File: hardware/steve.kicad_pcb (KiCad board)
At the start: 4 copper layers, 70 x 120 mm, 64 parts, among them J1 Conn_ARM_JTAG_SWD_10, J2 Micro_SD_Card_Det2, J3 TE_1-2834015-4_Buchanan_WireM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, J4 Screw_Terminal_01x04, J5 USB_C_Receptacle_16P, SW1 SW_SPST, SW2 SW_SPST, U1 STM32F407VGTx, U2 TI_TPS51386RJNR_Regulator_Buc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, U3 TLV1117LV33DCYR, U4 BMI270, U5 BMP388, Y1 12MHz, Y2 32.768kHz

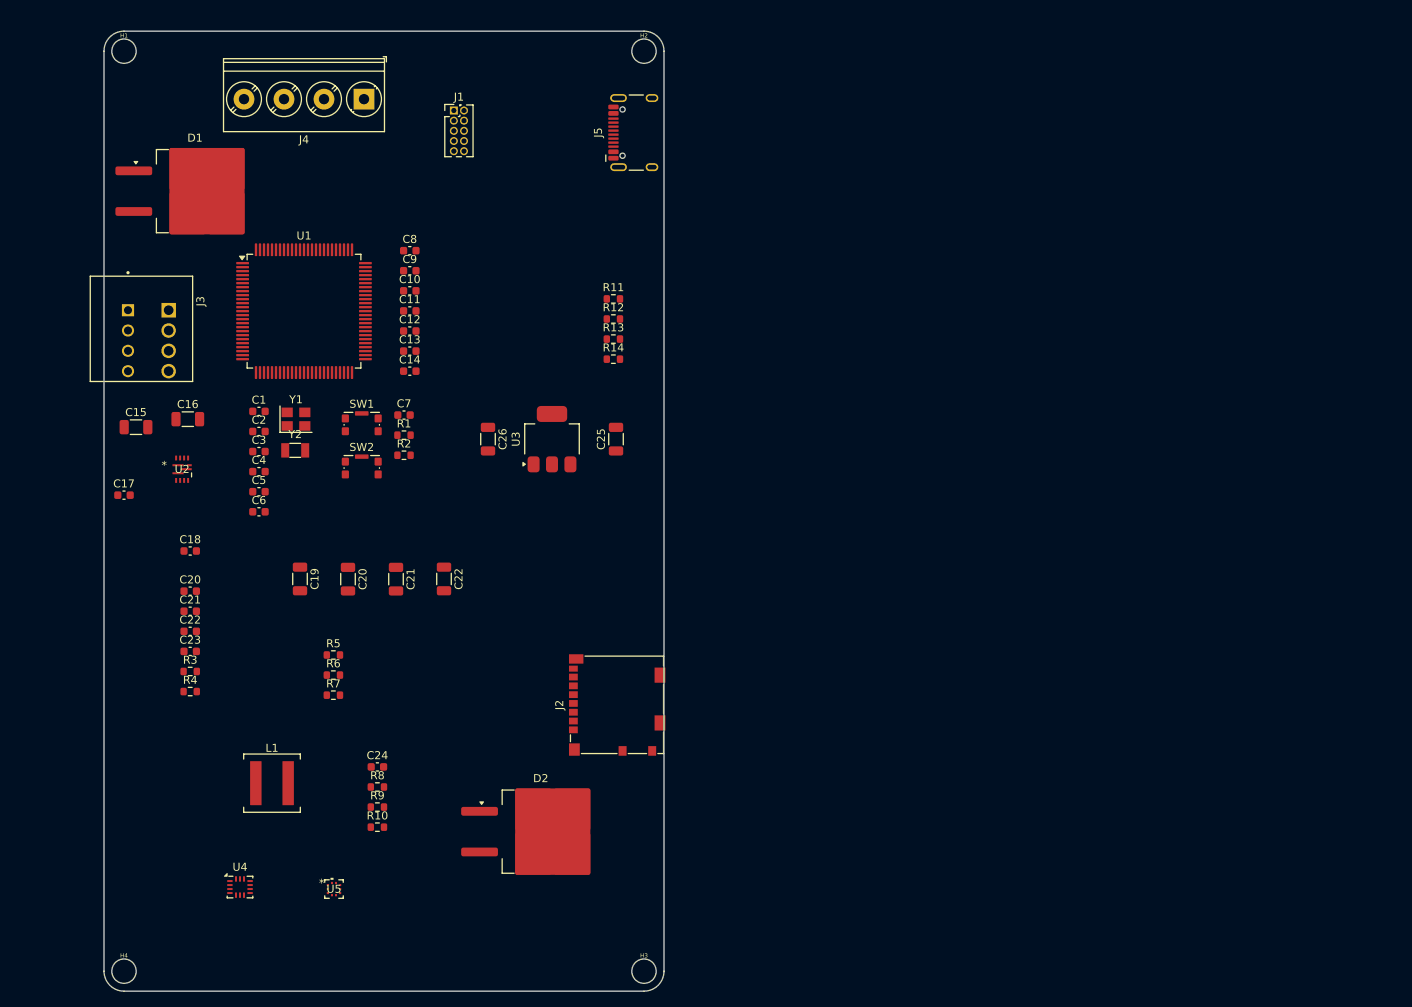
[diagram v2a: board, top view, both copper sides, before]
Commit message: Finished sensor, flash, and SD card in schematic; Updated README for remaining items
Finished BMI270 and BMP390, Flash storage, and  microSD card in schematic; Updated README for remaining items
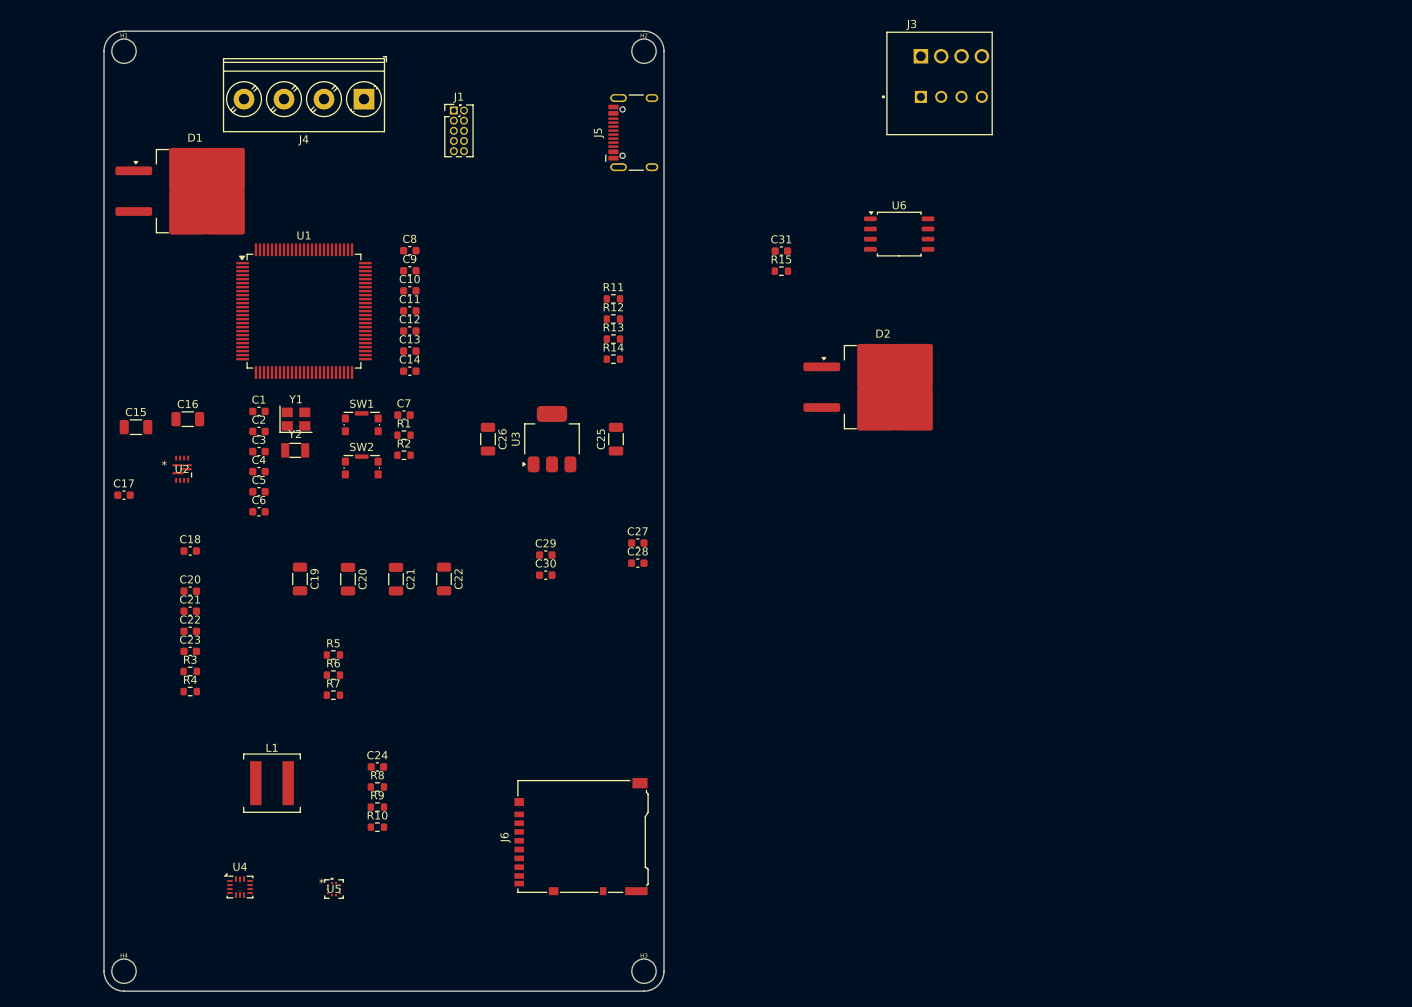
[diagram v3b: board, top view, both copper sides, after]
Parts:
- removed J2: Micro_SD_Card_Det2, Connector_Card:microSD_HC_Molex_104031-0811
- added C27: 0.1uF, Capacitor_SMD:C_0603_1608Metric, F.Cu at (116.7, 114.0)
- added C28: 0.1uF, Capacitor_SMD:C_0603_1608Metric, F.Cu at (116.7, 116.5)
- added C29: 0.1uF, Capacitor_SMD:C_0603_1608Metric, F.Cu at (105.2, 115.5)
- added C30: 0.1uF, Capacitor_SMD:C_0603_1608Metric, F.Cu at (105.2, 118.0)
- added C31: 0.1uF, Capacitor_SMD:C_0603_1608Metric, F.Cu at (134.7, 77.5)
- added J6: MicroSD_Hirose_DM3AT, Connector_Card:microSD_HC_Hirose_DM3AT-SF-PEJM5, F.Cu at (109.6, 150.7)
- added R15: 100k, Resistor_SMD:R_0603_1608Metric, F.Cu at (134.7, 80.0)
- added U6: W25Q128JVSIQ, Package_SO:SOIC-8_5.23x5.23mm_P1.27mm, F.Cu at (149.4, 75.4)
- U5: value BMP388 -> BMP388/390
- moved J3 105.7 mm to (155.9, 55.7), turned to 0 degrees
- moved D2 70.1 mm to (147.4, 94.5)
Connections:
- U1 pad 17: unconnected-(U1-PC2-Pad17) -> PC2_SPI2_MISO
- U1 pad 18: unconnected-(U1-PC3-Pad18) -> PC3_SPI2_MOSI
- U1 pad 29: unconnected-(U1-PA4-Pad29) -> PA4_BMI270_CS
- U1 pad 30: unconnected-(U1-PA5-Pad30) -> PA5_SPI1_SCK
- U1 pad 31: unconnected-(U1-PA6-Pad31) -> PA6_SPI1_MISO
- U1 pad 32: unconnected-(U1-PA7-Pad32) -> PA7_SPI1_MOSI
- U1 pad 35: unconnected-(U1-PB0-Pad35) -> PB0_BMP390_INT
- U1 pad 47: unconnected-(U1-PB10-Pad47) -> PB10_SPI2_SCK
- U1 pad 51: unconnected-(U1-PB12-Pad51) -> PB12_BMP390_CS
- U1 pad 65: unconnected-(U1-PC8-Pad65) -> SDIO_D0
- U1 pad 66: unconnected-(U1-PC9-Pad66) -> SDIO_D1
- U1 pad 77: unconnected-(U1-PA15-Pad77) -> FLASH_CS
- U1 pad 78: unconnected-(U1-PC10-Pad78) -> SDIO_D2
- U1 pad 79: unconnected-(U1-PC11-Pad79) -> SDIO_D3
- U1 pad 80: unconnected-(U1-PC12-Pad80) -> SDIO_CLK
- U1 pad 82: unconnected-(U1-PD1-Pad82) -> PD1_BMI270_INT
- U1 pad 83: unconnected-(U1-PD2-Pad83) -> SDIO_CMD
- U1 pad 89: unconnected-(U1-PB3-Pad89) -> FLASH_SCK
- U1 pad 90: unconnected-(U1-PB4-Pad90) -> FLASH_SDO
- U1 pad 91: unconnected-(U1-PB5-Pad91) -> FLASH_SDI
- U4 pad 1: unconnected-(U4-SDO-Pad1) -> PA6_SPI1_MISO
- U4 pad 12: unconnected-(U4-CSB-Pad12) -> PA4_BMI270_CS
- U4 pad 13: unconnected-(U4-SCx-Pad13) -> PA5_SPI1_SCK
- U4 pad 14: unconnected-(U4-SDx-Pad14) -> PA7_SPI1_MOSI
- U4 pad 4: unconnected-(U4-INT1-Pad4) -> PD1_BMI270_INT
- U4 pad 5: unconnected-(U4-VDDIO-Pad5) -> +3.3V
- U4 pad 6: unconnected-(U4-GNDIO-Pad6) -> GND
- U4 pad 7: unconnected-(U4-GND-Pad7) -> GND
- U4 pad 8: unconnected-(U4-VDD-Pad8) -> +3.3V
- U5 pad 1: unconnected-(U5-VDDIO-Pad1) -> +3.3V
- U5 pad 10: unconnected-(U5-VDD-Pad10) -> +3.3V
- U5 pad 2: unconnected-(U5-SCK-Pad2) -> PB10_SPI2_SCK
- U5 pad 3: unconnected-(U5-VSS-Pad3) -> GND
- U5 pad 4: unconnected-(U5-SDI-Pad4) -> PC3_SPI2_MOSI
- U5 pad 5: unconnected-(U5-SDO-Pad5) -> PC2_SPI2_MISO
- U5 pad 6: unconnected-(U5-CSB-Pad6) -> PB12_BMP390_CS
- U5 pad 7: unconnected-(U5-INT-Pad7) -> PB0_BMP390_INT
- U5 pad 8: unconnected-(U5-VSS-Pad8) -> GND
- U5 pad 9: unconnected-(U5-VSS-Pad9) -> GND

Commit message: Add components to schematic; fix existing ones
Added additional components to schematic such as IO connectors. Replaced the 10A TO-263-2 diode rectifiers with much smaller 5A ones.
Other various fixes.
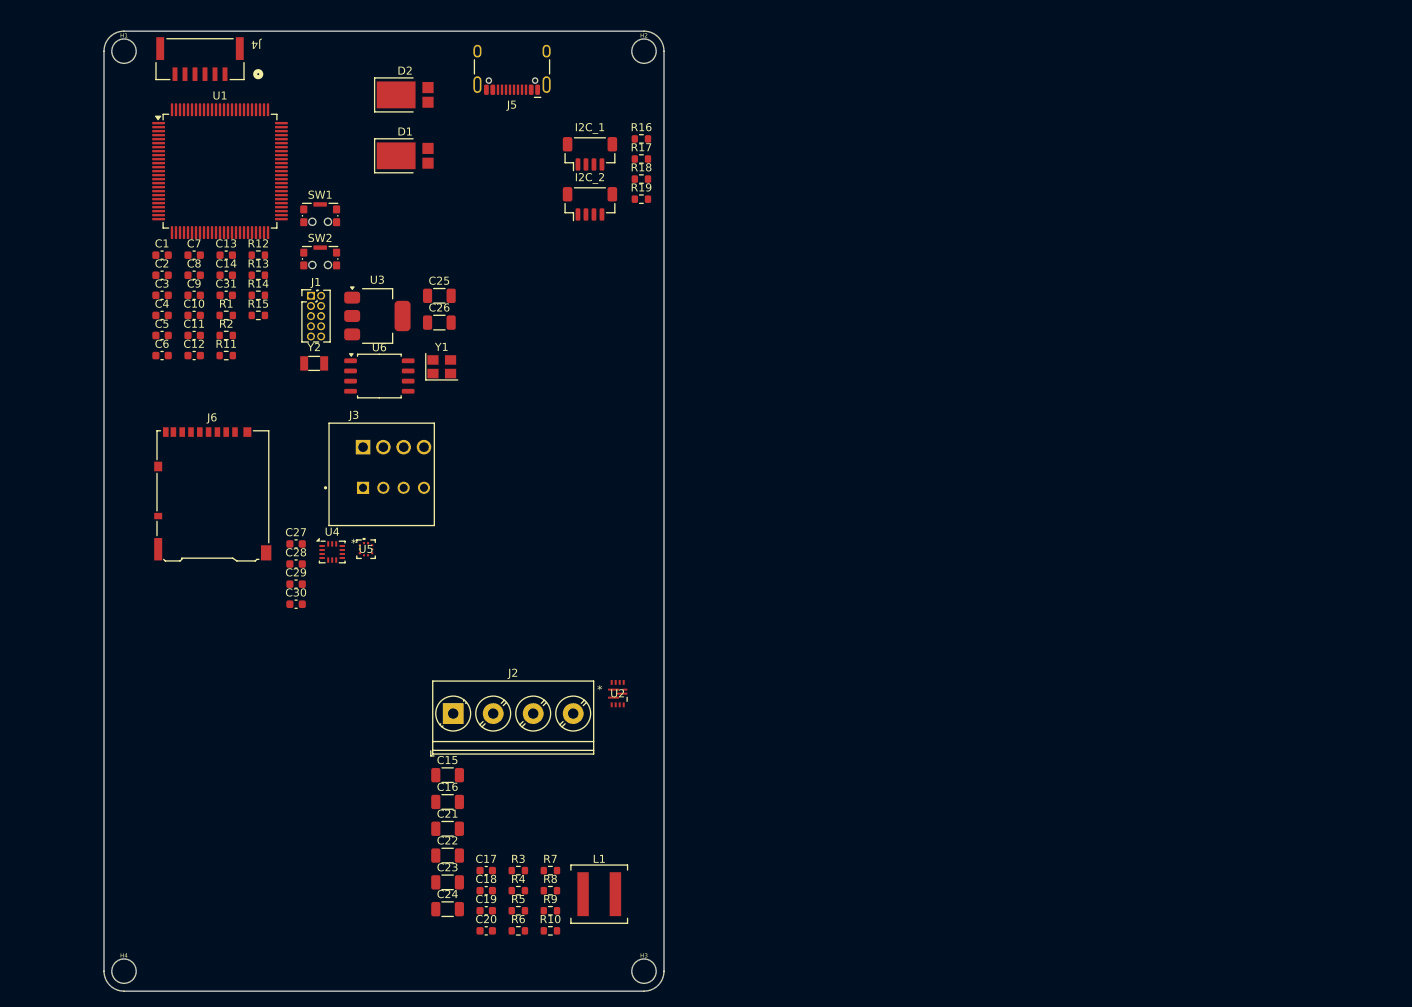
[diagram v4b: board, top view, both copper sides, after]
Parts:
- removed the C20 at (60.8, 120.0)
- removed the C20 at (80.5, 118.5)
- removed the C21 at (60.8, 122.5)
- removed the C21 at (86.5, 118.5)
- removed the C22 at (92.5, 118.5)
- removed the C22 at (60.8, 125.0)
- added C20: 22pF, Capacitor_SMD:C_0603_1608Metric, F.Cu at (97.8, 162.5)
- added C21: 22uF, Capacitor_SMD:C_1206_3216Metric, F.Cu at (93.0, 149.7)
- added C22: 22uF, Capacitor_SMD:C_1206_3216Metric, F.Cu at (93.0, 153.1)
- added I2C_1: JST-SH-4P, Imported_Footprints:JST-SH_BM04B-SRSS-TB_1x04_Vertical_P1.00mm, F.Cu at (110.7, 65.3)
- added I2C_2: JST-SH-4P, Imported_Footprints:JST-SH_BM04B-SRSS-TB_1x04_Vertical_P1.00mm, F.Cu at (110.7, 71.6)
- added J2: Screw_Terminal_01x04, TerminalBlock_Phoenix:TerminalBlock_Phoenix_PT-1,5-4-5.0-H_1x04_P5.00mm_Horizontal, F.Cu at (93.7, 135.3)
- added R16: 2k, Resistor_SMD:R_0603_1608Metric, F.Cu at (117.2, 63.5)
- added R17: 2k, Resistor_SMD:R_0603_1608Metric, F.Cu at (117.2, 66.0)
- added R18: 2k, Resistor_SMD:R_0603_1608Metric, F.Cu at (117.2, 68.5)
- added R19: 2k, Resistor_SMD:R_0603_1608Metric, F.Cu at (117.2, 71.0)
- C19: value 22uF -> 0.1uF; footprint Capacitor_SMD:C_1206_3216Metric -> Capacitor_SMD:C_0603_1608Metric
- C23: value 0.1uF -> 22uF; footprint Capacitor_SMD:C_0603_1608Metric -> Capacitor_SMD:C_1206_3216Metric
- C24: value 22pF -> 22uF; footprint Capacitor_SMD:C_0603_1608Metric -> Capacitor_SMD:C_1206_3216Metric
- D1: value RECTIFIER, SCHOTTKY, 10A per diode, 200V -> Schottky Diode Array, 5A per, 40V; footprint Package_TO_SOT_SMD:TO-263-2 -> Imported_Footprints:PDS1040CTL-13_PowerDI-5
- D2: value SCHOTTKY ARR, 10A per, 200V -> Schottky Diode Array, 5A per, 40V; footprint Package_TO_SOT_SMD:TO-263-2 -> Imported_Footprints:PDS1040CTL-13_PowerDI-5
- J4: value Screw_Terminal_01x04 -> JST-GH-6P_SM06B-GHS-TB; footprint TerminalBlock_Phoenix:TerminalBlock_Phoenix_PT-1,5-4-5.0-H_1x04_P5.00mm_Horizontal -> Imported_Footprints:CONN_JST-GH-6P_SM06B-GHS-TB
- R10: value 20k -> 120k
- R5: value 200k -> 20k
- R6: value 200k -> 0k
- R7: value 120k -> 150k
- R8: value 150k -> 200k
- R9: value 0k -> 200k
- moved J3 85.2 mm to (86.2, 104.5)
- moved D2 70.0 mm to (87.6, 58.0)
- moved C31 69.6 mm to (65.3, 83.0)
- moved U6 67.4 mm to (84.4, 93.1)
- moved R15 65.6 mm to (69.3, 85.5)
- moved C17 65.2 mm to (97.8, 154.9)
- moved J6 62.9 mm to (63.6, 107.8), turned to 0 degrees
- moved U2 61.2 mm to (114.2, 132.8)
- moved C15 58.4 mm to (93.0, 143.0)
- moved C16 57.8 mm to (93.0, 146.3)
- moved C18 56.3 mm to (97.8, 157.4)
- moved R11 48.9 mm to (65.3, 90.5)
- moved R3 48.0 mm to (101.8, 154.9)
- moved R4 48.0 mm to (101.8, 157.4)
- moved C19 47.6 mm to (97.8, 159.9), turned to 0 degrees
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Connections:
- C19 pad 1: +5V_BATT -> Net-(C19-Pad1)
- C19 pad 2: GND -> Net-(U2-SW)
- C23 pad 1: Net-(C23-Pad1) -> +5V_BATT
- C23 pad 2: Net-(U2-SW) -> GND
- C24 pad 1: Net-(C24-Pad1) -> +5V_BATT
- C24 pad 2: +5V_BATT -> GND
- J4 pad 1: +BATT_1 -> GND
- J4 pad 2: GND -> +5V
- J4 pad 3: +BATT_2 -> GND
- J4 pad 4: GND -> UART2_TX
- R10 pad 1: GND -> U2_EN
- R10 pad 2: U2_FB -> GND
- R4 pad 2: Net-(C23-Pad1) -> Net-(C19-Pad1)
- R5 pad 1: +BATT -> GND
- R5 pad 2: Net-(R5-Pad2) -> U2_FB
- R6 pad 1: Net-(R5-Pad2) -> U2_FB
- R6 pad 2: U2_EN -> Net-(C20-Pad1)
- R7 pad 1: U2_EN -> U2_FB
- R7 pad 2: GND -> +5V_BATT
- R8 pad 1: U2_FB -> +BATT
- R8 pad 2: +5V_BATT -> Net-(R8-Pad2)
- R9 pad 1: U2_FB -> Net-(R8-Pad2)
- R9 pad 2: Net-(C24-Pad1) -> U2_EN
- U1 pad 25: unconnected-(U1-PA2-Pad25) -> UART2_TX
- U1 pad 26: unconnected-(U1-PA3-Pad26) -> UART2_RX
- U1 pad 47: PB10_SPI2_SCK -> I2C2_SCL
- U1 pad 48: unconnected-(U1-PB11-Pad48) -> I2C2_SDA
- U1 pad 52: unconnected-(U1-PB13-Pad52) -> PB13_SPI2_SCK
- U1 pad 92: unconnected-(U1-PB6-Pad92) -> I2C1_SCL
- U1 pad 93: unconnected-(U1-PB7-Pad93) -> I2C1_SDA
- U5 pad 2: PB10_SPI2_SCK -> PB13_SPI2_SCK

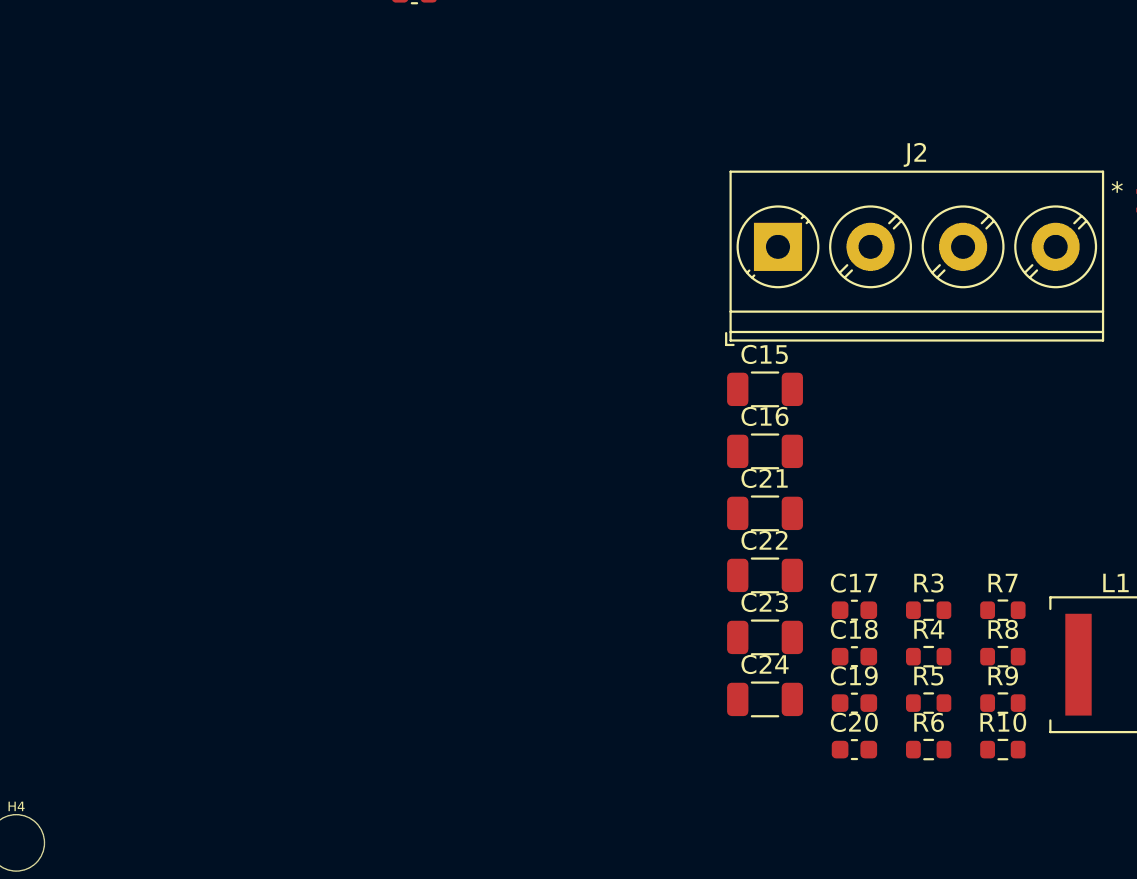
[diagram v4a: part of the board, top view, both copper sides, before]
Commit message: Added buzzer and LEDs to schematic
Added buzzer and LEDs (4 regular and 2 WS2812B) to schematic. Minor schematic fixes such as PMIC enable pin voltage divider.
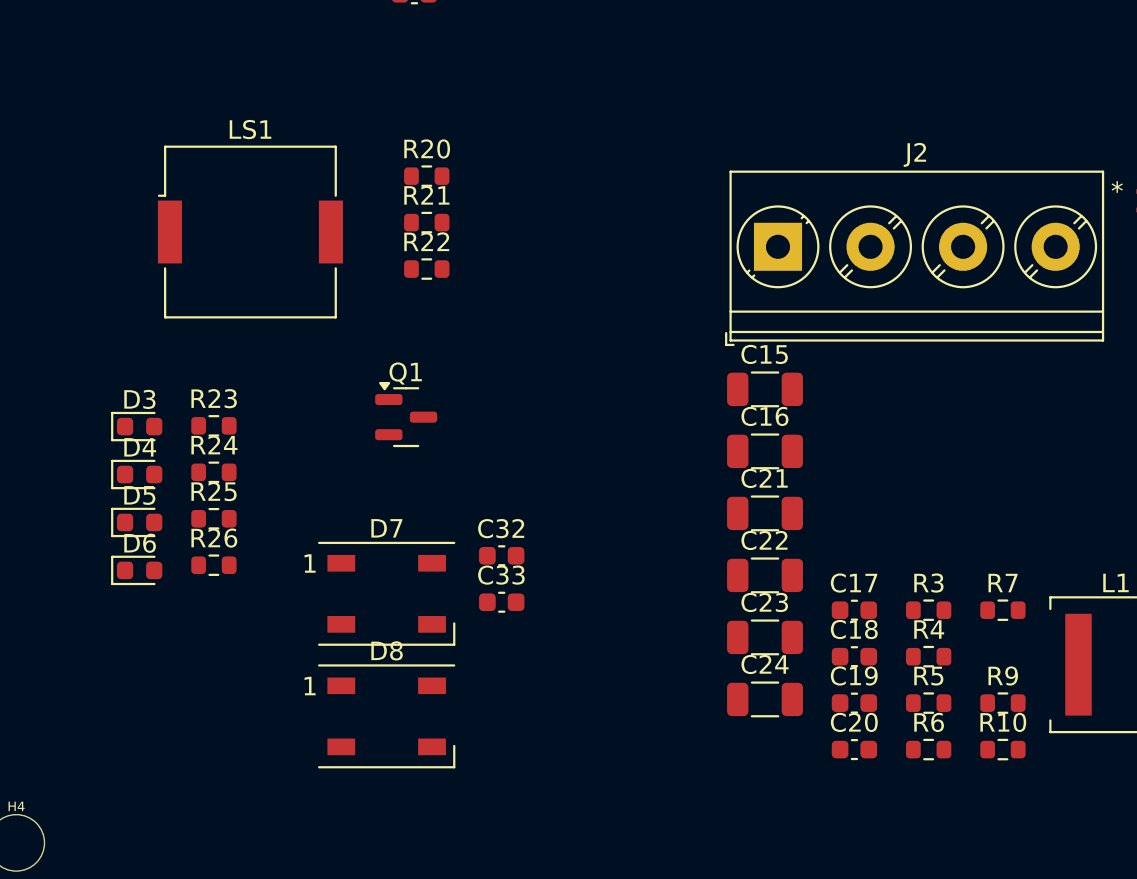
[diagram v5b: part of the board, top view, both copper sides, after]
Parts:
- removed R8: 200k, Resistor_SMD:R_0603_1608Metric
- added C32: 0.1uF, Capacitor_SMD:C_0603_1608Metric, F.Cu at (78.7, 152.0)
- added C33: 0.1uF, Capacitor_SMD:C_0603_1608Metric, F.Cu at (78.7, 154.5)
- added D3: RED, LED_SMD:LED_0603_1608Metric, F.Cu at (59.2, 145.0)
- added D4: Yellow, LED_SMD:LED_0603_1608Metric, F.Cu at (59.2, 147.6)
- added D5: GREEN, LED_SMD:LED_0603_1608Metric, F.Cu at (59.2, 150.2)
- added D6: BLUE, LED_SMD:LED_0603_1608Metric, F.Cu at (59.2, 152.8)
- added D7: WS2812B, LED_SMD:LED_WS2812B_PLCC4_5.0x5.0mm_P3.2mm, F.Cu at (72.5, 154.0)
- added D8: WS2812B, LED_SMD:LED_WS2812B_PLCC4_5.0x5.0mm_P3.2mm, F.Cu at (72.5, 160.7)
- added LS1: Speaker, Buzzer_Beeper:Buzzer_Murata_PKMCS0909E, F.Cu at (65.2, 134.5)
- added Q1: Q_NMOS_GSD, Package_TO_SOT_SMD:SOT-23, F.Cu at (73.6, 144.5)
- added R20: 1k, Resistor_SMD:R_0603_1608Metric, F.Cu at (74.7, 131.5)
- added R21: 1k, Resistor_SMD:R_0603_1608Metric, F.Cu at (74.7, 134.0)
- added R22: 1k, Resistor_SMD:R_0603_1608Metric, F.Cu at (74.7, 136.5)
- added R23: 220, Resistor_SMD:R_0603_1608Metric, F.Cu at (63.2, 145.0)
- added R24: 220, Resistor_SMD:R_0603_1608Metric, F.Cu at (63.2, 147.5)
- added R25: 220, Resistor_SMD:R_0603_1608Metric, F.Cu at (63.2, 150.0)
- added R26: 1k, Resistor_SMD:R_0603_1608Metric, F.Cu at (63.2, 152.5)
- R10: value 120k -> 100k 1%
- R4, R6: value 0k -> 0k 1%
- R5: value 20k -> 20k 1%
- R7: value 150k -> 150k 1%
- R9: value 200k -> 330k 1%
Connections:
- R9 pad 1: Net-(R8-Pad2) -> +BATT
- U1 pad 4: unconnected-(U1-PE5-Pad4) -> Buzzer
- U1 pad 58: unconnected-(U1-PD11-Pad58) -> LED_WS2812
- U1 pad 59: unconnected-(U1-PD12-Pad59) -> LED1
- U1 pad 60: unconnected-(U1-PD13-Pad60) -> LED2
- U1 pad 61: unconnected-(U1-PD14-Pad61) -> LED3
- U1 pad 62: unconnected-(U1-PD15-Pad62) -> LED4
